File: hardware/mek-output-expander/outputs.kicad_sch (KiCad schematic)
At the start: 86 parts, among them J4 Screw_Terminal_01x02, J5 Screw_Terminal_01x02, J6 Screw_Terminal_01x02, J7 Screw_Terminal_01x02, J8 Screw_Terminal_01x02, Q1 BT136S-800E, Q2 BT136S-800E, Q3 BT136S-800E, Q4 BT136S-800E, Q5 BT136S-800E, Q6 BT136S-800E, Q7 BT136S-800E, Q8 BT136S-800E, U10 MOC3063S, U11 MOC3063S, U12 MOC3063S, U13 MOC3063S, U14 MOC3063S, U6 ULN2803A, U7 MOC3063S, U8 MOC3063S, U9 MOC3063S

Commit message: Board, scripts and 3d model updates
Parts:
- U6: footprint Package_SO:SOP-18_7.495x11.515mm_P1.27mm -> Package_SO:SOIC-18W_7.5x11.6mm_P1.27mm
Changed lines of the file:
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@@
 			)
 		)
-		(property "Footprint" "Package_SO:SOP-18_7.495x11.515mm_P1.27mm"
+		(property "Footprint" "Package_SO:SOIC-18W_7.5x11.6mm_P1.27mm"
 			(at 54.61 48.26 0)
 			(hide yes)

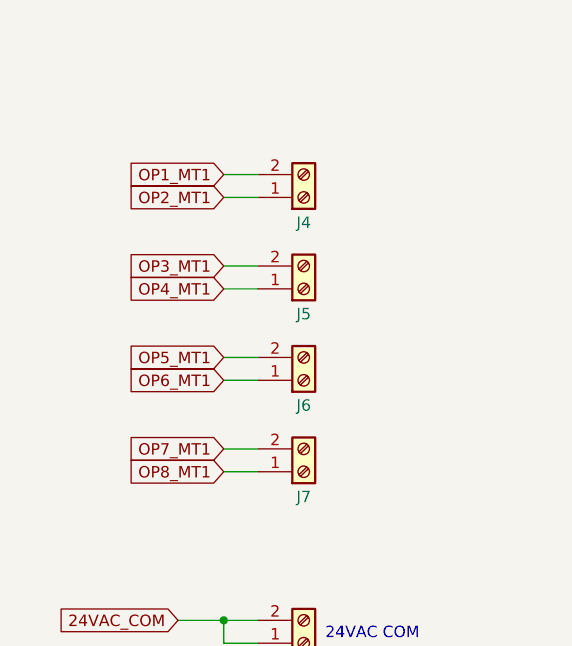
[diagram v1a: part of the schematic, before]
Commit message: Configure net classes + board stack up changes for edge script
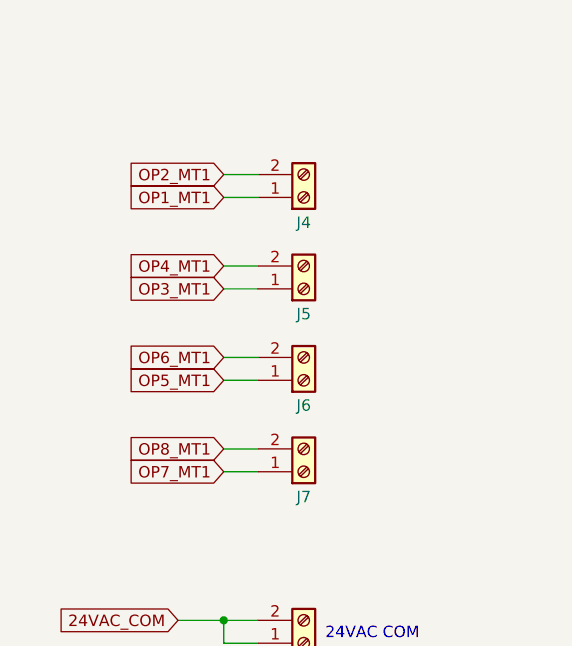
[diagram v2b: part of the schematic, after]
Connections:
- net OP1_MT1: now also J4.1 (Pin_1); no longer J4.2 (Pin_2)
- net OP2_MT1: now also J4.2 (Pin_2); no longer J4.1 (Pin_1)
- net OP3_MT1: now also J5.1 (Pin_1); no longer J5.2 (Pin_2)
- net OP4_MT1: now also J5.2 (Pin_2); no longer J5.1 (Pin_1)
- net OP5_MT1: now also J6.1 (Pin_1); no longer J6.2 (Pin_2)
- net OP6_MT1: now also J6.2 (Pin_2); no longer J6.1 (Pin_1)
- net OP7_MT1: now also J7.1 (Pin_1); no longer J7.2 (Pin_2)
- net OP8_MT1: now also J7.2 (Pin_2); no longer J7.1 (Pin_1)
